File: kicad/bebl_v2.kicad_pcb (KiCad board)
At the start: 2 copper layers, 80 x 39 mm, 78 parts, among them P1 ISP, P10 LED_DRL, P11 DRV_LED, P12 CHG_LED, P13 LED_CHG, P2 FTDI, P3 LiPo, P4 USB-Micro, P5 Alt_Add, P6 Int1, P7 Int2, P8 DRL_LED, P9 LED_DRV, SW1 RST, SW2 MODE, U1 ATMEGA328, U2 FAN5346, U3 ADXL345, U4 MCP73831, U5 TPS61221DCK, X1 8MHz

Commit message: bebl_v2 3d of housing, work in progress
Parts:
- moved P3 6.02 mm to (99.5, 42.5), turned to 270 degrees
- moved SC1 0.71 mm to (40.5, 59.5)
- moved SC10 0.71 mm to (55.0, 74.5)
- moved SC11 0.71 mm to (110.0, 74.5)
- moved SC12 0.71 mm to (110.0, 65.5)
- moved SC2 0.71 mm to (115.5, 40.5)
- moved SC3 0.71 mm to (115.5, 59.5)
- moved SC4 0.71 mm to (40.5, 40.5)
- moved SC5 0.71 mm to (55.0, 54.5)
- moved SC6 0.71 mm to (55.0, 45.5)
- moved SC7 0.71 mm to (110.0, 45.5)
- moved SC8 0.71 mm to (110.0, 54.5)
- moved SC9 0.71 mm to (55.0, 65.5)
- moved B14 0.50 mm to (97.5, 50.0)
- moved B15 0.50 mm to (50.5, 50.0)
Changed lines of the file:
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@@
-(kicad_pcb (version 4) (host pcbnew "(2014-09-25 BZR 5147)-product")
+(kicad_pcb (version 4) (host pcbnew "(2014-jul-16 BZR unknown)-product")
   (general
     (links 143)
     (no_connects 143)
-    (area 37.8537 37.5442 118.521201 77.075001)
+    (area 36.399999 35.7817 119.600001 77.075001)
     (thickness 1.6)
-    (drawings 12)
+    (drawings 24)
     (tracks 0)
     (zones 0)
@@
   )
   (module bebl_v2_pretty:batt_clip (layer B.Cu)
-    (at 98 50 180)
+    (at 97.5 50 180)
     (fp_text reference B14 (at 3.556 0 450) (layer B.SilkS)
       (effects (font (size 1.5 1.5) (thickness 0.15)) (justify mirror))
@@
   )
   (module bebl_v2_pretty:batt_clip (layer B.Cu)
-    (at 50 50)
+    (at 50.5 50)
     (fp_text reference B15 (at 3.556 0 270) (layer B.SilkS)
       (effects (font (size 1.5 1.5) (thickness 0.15)) (justify mirror))
@@
   )
   (module bebl_v2_pretty:screw_3mm (layer F.Cu)
-    (at 110.5 65)
+    (at 110 65.5)
     (descr "vite 2,5mm")
     (fp_text reference SC12 (at 0 1.0795) (layer F.SilkS) hide
@@
   )
   (module bebl_v2_pretty:screw_3mm (layer F.Cu)
-    (at 110.5 75)
+    (at 110 74.5)
     (descr "vite 2,5mm")
     (fp_text reference SC11 (at 0 1.0795) (layer F.SilkS) hide
@@
   )
   (module bebl_v2_pretty:screw_3mm (layer F.Cu)
-    (at 54.5 75)
+    (at 55 74.5)
     (descr "vite 2,5mm")
     (fp_text reference SC10 (at 0 1.0795) (layer F.SilkS) hide
@@
   )
   (module bebl_v2_pretty:screw_3mm (layer F.Cu)
-    (at 54.5 65)
+    (at 55 65.5)
     (descr "vite 2,5mm")
     (fp_text reference SC9 (at 0 1.0795) (layer F.SilkS) hide
@@
   )
   (module bebl_v2_pretty:screw_3mm (layer F.Cu)
-    (at 110.5 55)
+    (at 110 54.5)
     (descr "vite 2,5mm")
     (fp_text reference SC8 (at 0 1.0795) (layer F.SilkS) hide
@@
   )
   (module bebl_v2_pretty:screw_3mm (layer F.Cu)
-    (at 110.5 45)
+    (at 110 45.5)
     (descr "vite 2,5mm")
     (fp_text reference SC7 (at 0 1.0795) (layer F.SilkS) hide
@@
   )
   (module bebl_v2_pretty:screw_3mm (layer F.Cu)
-    (at 54.5 45)
+    (at 55 45.5)
     (descr "vite 2,5mm")
     (fp_text reference SC6 (at 0 1.0795) (layer F.SilkS) hide
@@
   )
   (module bebl_v2_pretty:screw_3mm (layer F.Cu)
-    (at 54.5 55)
+    (at 55 54.5)
     (descr "vite 2,5mm")
     (fp_text reference SC5 (at 0 1.0795) (layer F.SilkS) hide
@@
   )
   (module bebl_v2_pretty:screw_3mm (layer F.Cu)
-    (at 40 60)
+    (at 40.5 59.5)
     (descr "vite 2,5mm")
     (fp_text reference SC1 (at 0 1.0795) (layer F.SilkS) hide
@@
   )
   (module bebl_v2_pretty:screw_3mm (layer F.Cu)
-    (at 116 40)
+    (at 115.5 40.5)
     (descr "vite 2,5mm")
     (fp_text reference SC2 (at 0 1.0795) (layer F.SilkS) hide
@@
   )
   (module bebl_v2_pretty:screw_3mm (layer F.Cu)
-    (at 116 60)
+    (at 115.5 59.5)
     (descr "vite 2,5mm")
     (fp_text reference SC3 (at 0 1.0795) (layer F.SilkS) hide
@@
   )
   (module bebl_v2_pretty:screw_3mm (layer F.Cu)
-    (at 40 40)
+    (at 40.5 40.5)
     (descr "vite 2,5mm")
     (fp_text reference SC4 (at 0 1.0795) (layer F.SilkS) hide
@@
   )
   (module bebl_v2_pretty:CONN_JST-2_SMD (layer F.Cu)
-    (at 104 38.5 180)
+    (at 99.5 42.5 270)
     (tags JST)
-    (fp_text reference P3 (at -5.5245 -7.747 450) (layer F.SilkS)
+    (fp_text reference P3 (at -5.5245 -7.747 540) (layer F.SilkS)
       (effects (font (size 1.016 1.016) (thickness 0.1524)))
     )
-    (fp_text value LiPo (at -5.5245 -2.9845 450) (layer F.SilkS)
+    (fp_text value LiPo (at -5.5245 -2.9845 540) (layer F.SilkS)
       (effects (font (size 1.016 1.016) (thickness 0.1524)))
     )
@@
     (fp_line (start 3.4925 -8.5725) (end 4.445 -8.5725) (layer F.SilkS) (width 0.1524))
     (fp_line (start 4.445 0.381) (end 0 0.381) (layer F.SilkS) (width 0.1524))
-    (pad "" smd rect (at -3.34772 -1.69926 180) (size 1.4986 3.39598) (layers F.Cu F.Paste F.Mask))
-    (pad 1 smd rect (at -0.99822 -7.24916 180) (size 0.99568 3.49758) (layers F.Cu F.Paste F.Mask)
+    (pad "" smd rect (at -3.34772 -1.69926 270) (size 1.4986 3.39598) (layers F.Cu F.Paste F.Mask))
+    (pad 1 smd rect (at -0.99822 -7.24916 270) (size 0.99568 3.49758) (layers F.Cu F.Paste F.Mask)
       (net 13 /BAT))
-    (pad 2 smd rect (at 0.99822 -7.24916 180) (size 0.99568 3.49758) (layers F.Cu F.Paste F.Mask)
-      (net 14 GND))
-    (pad "" smd rect (at 3.34772 -1.69926 180) (size 1.4986 3.39598) (layers F.Cu F.Paste F.Mask))
+    (pad 2 smd rect (at 0.99822 -7.24916 270) (size 0.99568 3.49758) (layers F.Cu F.Paste F.Mask)
+      (net 14 GND))
+    (pad "" smd rect (at 3.34772 -1.69926 270) (size 1.4986 3.39598) (layers F.Cu F.Paste F.Mask))
     (model /home/samata/projects-git/bebl_v2/kicad/3d_modules/s2b-ph-sm4-tb.wrl
       (at (xyz 0 0.254 0))
@@
     )
   )
+  (gr_line (start 38 43) (end 38 38) (angle 90) (layer Dwgs.User) (width 0.2))
+  (gr_line (start 43 43) (end 38 43) (angle 90) (layer Dwgs.User) (width 0.2))
+  (gr_line (start 43 38) (end 43 43) (angle 90) (layer Dwgs.User) (width 0.2))
+  (gr_line (start 38 38) (end 43 38) (angle 90) (layer Dwgs.User) (width 0.2))
+  (gr_line (start 118 38) (end 113 38) (angle 90) (layer Dwgs.User) (width 0.2))
+  (gr_line (start 118 43) (end 118 38) (angle 90) (layer Dwgs.User) (width 0.2))
+  (gr_line (start 113 43) (end 118 43) (angle 90) (layer Dwgs.User) (width 0.2))
+  (gr_line (start 113 38) (end 113 43) (angle 90) (layer Dwgs.User) (width 0.2))
+  (gr_line (start 119.5 63.5) (end 119.5 36.5) (angle 90) (layer Dwgs.User) (width 0.2))
+  (gr_line (start 36.5 63.5) (end 119.5 63.5) (angle 90) (layer Dwgs.User) (width 0.2))
+  (gr_line (start 36.5 36.5) (end 36.5 63.5) (angle 90) (layer Dwgs.User) (width 0.2))
+  (gr_line (start 119.5 36.5) (end 36.5 36.5) (angle 90) (layer Dwgs.User) (width 0.2))
   (gr_line (start 52.5 63) (end 77.5 63) (angle 90) (layer Edge.Cuts) (width 0.15))
   (gr_line (start 77.5 62) (end 38 62) (angle 90) (layer Edge.Cuts) (width 0.15))

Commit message: working on case for bebl_v2
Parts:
- removed B8, B9: I/O, bebl_v2_pretty:breakout_smd
- removed P5: Alt_Add, bebl_v2_pretty:solder_bridge_3
- removed P6: Int1, bebl_v2_pretty:solder_bridge_3
- removed P7: Int2, bebl_v2_pretty:solder_bridge_3
- moved P3 12.0 mm to (87.5, 42.5)
- moved P1 4.00 mm to (67.5, 39.5)
- moved R1 4.00 mm to (87.0, 60.0)
- moved C12 3.50 mm to (83.0, 53.5)
- moved C8 3.50 mm to (91.0, 53.5)
- moved R6 3.50 mm to (87.0, 57.0)
- moved R7 3.50 mm to (87.0, 50.0)
- moved U4 3.50 mm to (87.0, 53.5)
- moved C10 2.00 mm to (77.0, 49.0)
- moved C7 2.00 mm to (77.0, 55.0)
- moved L2 2.00 mm to (72.5, 52.0)
- moved U5 2.00 mm to (77.0, 52.0)
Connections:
- P4 pad 2: Net-(P4-Pad2) -> (no net)
- P4 pad 3: Net-(P4-Pad3) -> (no net)
- P4 pad 4: Net-(P4-Pad4) -> (no net)
- R8 pad 2: /INT0 -> /MODE
- SW2 pad 2: /INT0 -> /MODE
- U1 pad 1: Net-(B8-Pad1) -> /ACL_INT2
- U1 pad 2: Net-(B9-Pad1) -> /MODE
- U1 pad 32: /INT0 -> /ACL_INT1
- U3 pad 10: Net-(U3-Pad10) -> (no net)
- U3 pad 11: Net-(U3-Pad11) -> (no net)
- U3 pad 12: /ACL_SDO -> GND
- U3 pad 3: Net-(U3-Pad3) -> (no net)

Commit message: bebl_v2 track layout, work in progress
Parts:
- removed B1, B10, B11, B12, B13, B2, B3, B4, B5, B6: I/O, bebl_v2_pretty:breakout_smd
- removed SC10, SC11, SC12, SC9: SCREW, bebl_v2_pretty:screw_3mm
- P3: footprint bebl_v2_pretty:CONN_JST-2_SMD -> bebl_v2_pretty:pin_strip_2
- moved C3 20.8 mm to (60.5, 58.0), turned to 0 degrees
- moved R2 18.1 mm to (79.5, 41.0), turned to 90 degrees
- moved P9 17.6 mm to (37.0, 72.0)
- moved P11 17.5 mm to (37.0, 50.0)
- moved P8 17.4 mm to (93.5, 46.5)
- moved P10 17.1 mm to (93.5, 68.5)
- moved D6 16.1 mm to (44.0, 72.0)
- moved SC5 15.2 mm to (40.0, 57.0)
- moved SC6 15.2 mm to (40.0, 43.0)
- moved R3 14.8 mm to (82.0, 41.0), turned to 90 degrees
- moved R4 14.2 mm to (88.5, 56.5)
- moved D5 13.6 mm to (54.0, 72.0)
- moved C4 12.5 mm to (79.5, 55.5)
- moved R6 12.2 mm to (78.5, 48.2)
- moved D4 11.2 mm to (64.0, 72.0)
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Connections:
- P4 pad 2: (no net) -> Net-(P4-Pad2)
- P4 pad 3: (no net) -> Net-(P4-Pad3)
- P4 pad 4: (no net) -> Net-(P4-Pad4)
- U1 pad 1: /ACL_INT2 -> /ACL_INT1
- U1 pad 32: /ACL_INT1 -> /ACL_INT2
- U3 pad 10: (no net) -> Net-(U3-Pad10)
- U3 pad 11: (no net) -> Net-(U3-Pad11)
- U3 pad 3: (no net) -> Net-(U3-Pad3)
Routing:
- net GND: track 0.00 -> 245.7 mm, vias 0 -> 5
- net +3.3V: track 0.00 -> 106.4 mm, vias 0 -> 2
- net /BAT: track 0.00 -> 71.2 mm, vias 0 -> 1
- net /CATH: track 0.00 -> 48.8 mm
- net /RESET: track 0.00 -> 40.8 mm, vias 0 -> 2
- net /VUSB: track 0.00 -> 33.8 mm
- net /MODE: track 0.00 -> 26.8 mm, vias 0 -> 1
- net /LED_A: track 0.00 -> 26.5 mm
- net /DRL_PWM: track 0.00 -> 25.5 mm, vias 0 -> 2
- net /LED_K: track 0.00 -> 25.4 mm
- net Net-(P12-Pad2): track 0.00 -> 20.9 mm
- net /SCL: track 0.00 -> 20.1 mm, vias 0 -> 2
- net /PB7: track 0.00 -> 19.0 mm
- net /ACL_INT1: track 0.00 -> 18.5 mm, vias 0 -> 2
- net /PB6: track 0.00 -> 17.1 mm
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- added copper zone on B.Cu, net GND
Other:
- board size 80 x 39 mm -> 80 x 41 mm
- net class 0.2mm added: clearance 0.2, trace_width 0.2, via_dia 0.889, via_drill 0.635
- net class Default: clearance 0.254 -> 0.25; trace_width 0.254 -> 0.3
- rule trace_clearance: 0.254 -> 0.25
- rule trace_min: 0.254 -> 0.2

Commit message: working on case for bebl_v2
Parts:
- added B1: I/O, bebl_v2_pretty:breakout_smd, B.Cu at (75.1, 43.1)
- added B10: I/O, bebl_v2_pretty:breakout_smd, B.Cu at (64.9, 51.0)
- added B11: I/O, bebl_v2_pretty:breakout_smd, B.Cu at (64.0, 49.8)
- added B12: I/O, bebl_v2_pretty:breakout_smd, B.Cu at (63.4, 48.4)
- added B13: I/O, bebl_v2_pretty:breakout_smd, B.Cu at (63.3, 46.9)
- added B2: I/O, bebl_v2_pretty:breakout_smd, B.Cu at (76.6, 43.1)
- added B3: I/O, bebl_v2_pretty:breakout_smd, B.Cu at (77.9, 45.3)
- added B4: I/O, bebl_v2_pretty:breakout_smd, B.Cu at (77.9, 46.8)
- added B5: I/O, bebl_v2_pretty:breakout_smd, B.Cu at (69.6, 43.5)
- added B6: I/O, bebl_v2_pretty:breakout_smd, B.Cu at (73.6, 43.1)
- P3: value LiPo -> Ext_LiPo; moved to B.Cu
- moved R7 3.00 mm to (78.5, 48.5)
- moved R6 2.70 mm to (78.5, 45.5)
- moved U4 2.50 mm to (78.5, 52.0)
- moved C4 1.58 mm to (80.0, 57.0), turned to 180 degrees
- moved C12 1.50 mm to (74.5, 52.0)
- moved C6 0.50 mm to (55.0, 53.0)
- moved R4 0.50 mm to (88.5, 57.0)
- moved R5 0.50 mm to (55.0, 47.0)
- moved L1 0.40 mm to (62.0, 52.1)
- moved C8 0.30 mm to (82.5, 52.0)
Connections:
- C5 pad 1: /VLED -> +3.3V
- L1 pad 1: /VLED -> +3.3V
- P4 pad 2: Net-(P4-Pad2) -> (no net)
- P4 pad 3: Net-(P4-Pad3) -> (no net)
- P4 pad 4: Net-(P4-Pad4) -> (no net)
- U2 pad 1: /VLED -> +3.3V
- U3 pad 10: Net-(U3-Pad10) -> (no net)
- U3 pad 11: Net-(U3-Pad11) -> (no net)
- U3 pad 3: Net-(U3-Pad3) -> (no net)
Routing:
- net GND: track 245.7 -> 283.8 mm
- net /ACL_INT2: track 0.00 -> 15.3 mm, vias 0 -> 2
- net +3.3V: track 106.4 -> 115.3 mm
- net /VLED: track 5.77 -> 0.00 mm
- net Net-(B1-Pad1): track 0.00 -> 4.50 mm
- net Net-(B2-Pad1): track 0.00 -> 4.41 mm
- net /SS: track 0.00 -> 4.34 mm
- net Net-(B3-Pad1): track 0.00 -> 4.04 mm
- net Net-(B12-Pad1): track 0.00 -> 3.95 mm
- net Net-(B4-Pad1): track 0.00 -> 3.66 mm
- net Net-(B6-Pad1): track 0.00 -> 3.33 mm
- net Net-(B11-Pad1): track 0.00 -> 3.10 mm
- net /ACL_INT1: track 18.5 -> 15.5 mm
- net Net-(P12-Pad2): track 20.9 -> 23.4 mm
- net /SDA: track 16.4 -> 13.9 mm
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- added copper zone on F.Cu, net /D1K
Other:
- board text added: "(3V3)"
- board text added: "BLK"
- board text added: "BicyclE Brake Light"
- board text added: "GRN"
- board text added: "[+ -]"
- board text added: "[+]"
- board text added: "[-]"
- board text added: "bebl_v2"
- board text added: "www.wyolum.com"

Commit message: work in progress
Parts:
- moved D1 3.00 mm to (104.0, 75.0)
- moved D2 3.00 mm to (84.0, 75.0)
- moved D3 3.00 mm to (74.0, 75.0)
- moved D4 3.00 mm to (64.0, 75.0)
- moved D5 3.00 mm to (54.0, 75.0)
- moved D6 3.00 mm to (44.0, 75.0)
- moved D8 3.00 mm to (94.0, 75.0)
- moved P10 3.00 mm to (93.5, 71.5)
- moved P13 3.00 mm to (93.5, 78.5)
- moved P9 3.00 mm to (37.0, 75.0)
- turned P3 to 180 degrees
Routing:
- net /BAT: track 72.4 -> 67.4 mm
- net GND: track 283.8 -> 285.9 mm
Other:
- board size 80 x 41 mm -> 80 x 44 mm
- board text added: "[- +]"
- board text removed: "[+ -]"

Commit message: bebl_v2 box stl files ready for prototype
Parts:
- moved P4 0.10 mm to (109.9, 50.0)

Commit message: modified schematic for transistor drive
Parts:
- renumbered P4 to P7, P12 to P8

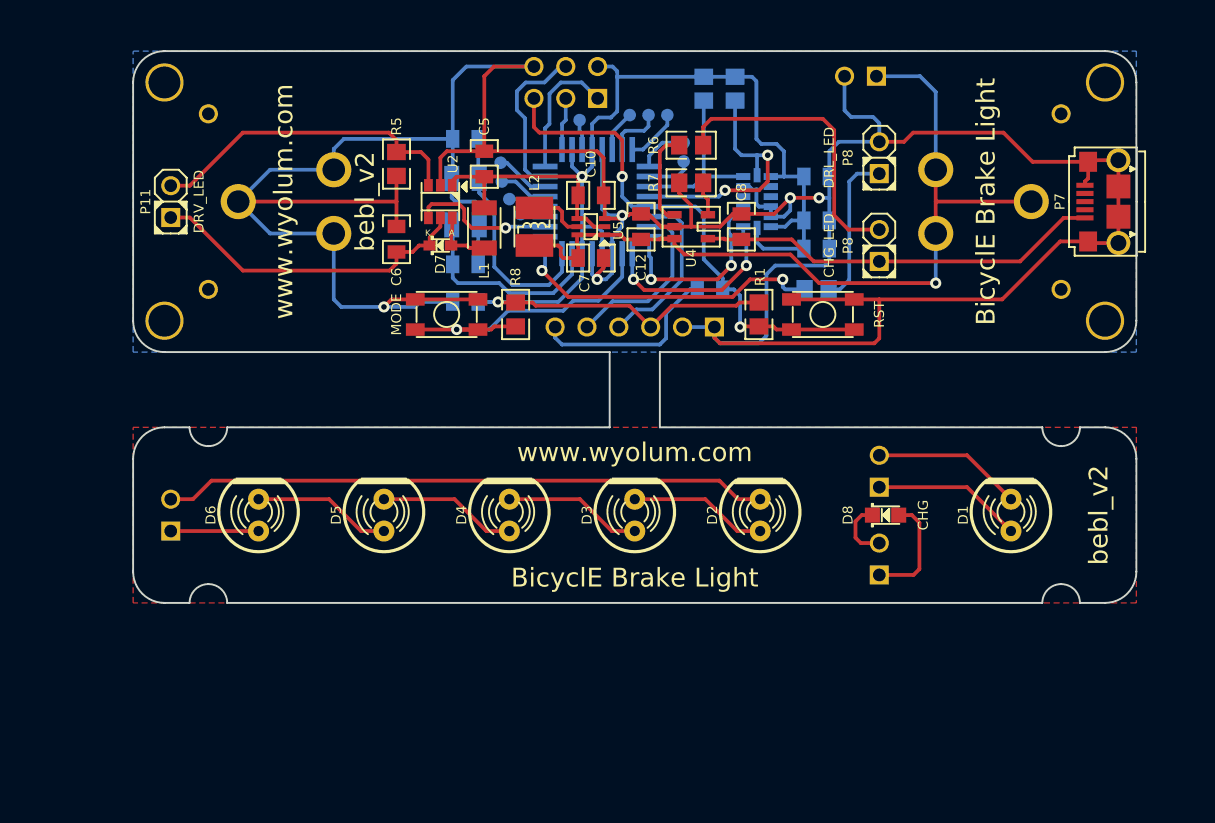
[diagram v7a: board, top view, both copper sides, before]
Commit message: new LED drive circuit, work in progress
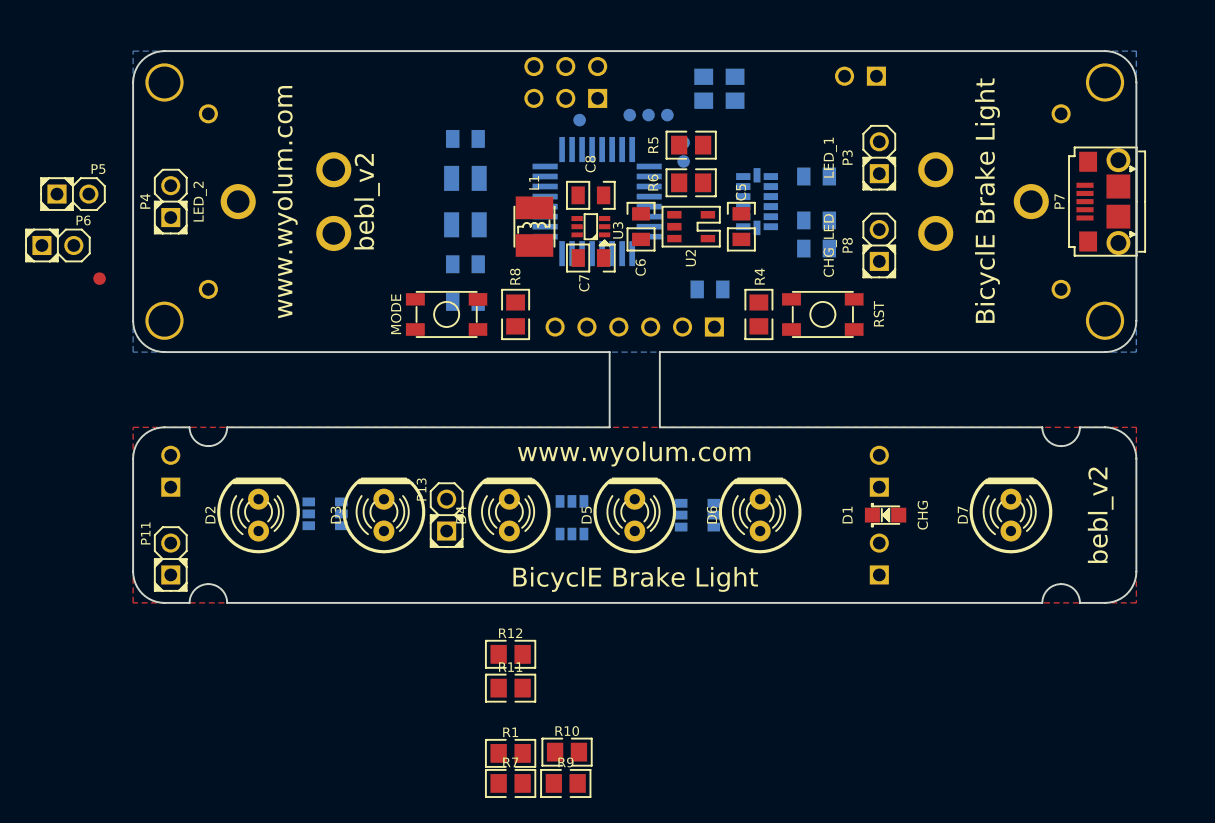
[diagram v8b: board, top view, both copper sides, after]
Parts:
- removed B10, B11, B12, B13: I/O, bebl_v2_pretty:breakout_smd
- removed the C5 at (62.0, 47.0)
- removed the C6 at (55.0, 53.0)
- removed the D7 at (58.5, 53.5)
- removed the L1 at (62.0, 52.1)
- removed the P3 at (92.0, 40.0)
- removed the R4 at (88.5, 57.0)
- removed the R5 at (55.0, 47.0)
- removed the U2 at (58.5, 50.0)
- added B7: I/O, bebl_v2_pretty:breakout_smd, F.Cu at (31.3, 56.1)
- added P10: LED_CHG, bebl_v2_pretty:pin_strip_2, B.Cu at (93.5, 78.5)
- added P11: LED_1, bebl_v2_pretty:pin_strip_2, F.Cu at (37.0, 78.5)
- added P12: LED_2, bebl_v2_pretty:pin_strip_2, B.Cu at (37.0, 71.5)
- added P5: LED_3, bebl_v2_pretty:pin_socket_2, F.Cu at (29.2, 49.4)
- added P6: LED_PWR, bebl_v2_pretty:pin_socket_2, F.Cu at (28.0, 53.5)
- added Q1: BC847BDW1T1G, bebl_v2_pretty:SOT23-6, B.Cu at (79.0, 75.0)
- added Q2: BC847BDW1T1G, bebl_v2_pretty:SOT23-6, B.Cu at (49.3, 74.9)
- added Q3: BC847BDW1T1G, bebl_v2_pretty:SOT23-6, B.Cu at (69.0, 75.2)
- added R1: 10k, bebl_v2_pretty:r_0805, F.Cu at (64.1, 94.0)
- added R10: 56E, bebl_v2_pretty:r_0805, F.Cu at (68.6, 93.9)
- added R11: 56E, bebl_v2_pretty:r_0805, F.Cu at (64.1, 88.8)
- added R12: 56E, bebl_v2_pretty:r_0805, F.Cu at (64.1, 86.1)
- added R7: 56E, bebl_v2_pretty:r_0805, F.Cu at (64.1, 96.4)
- added R9: 56E, bebl_v2_pretty:r_0805, F.Cu at (68.5, 96.4)
- D2: renamed from D6; value LED_R -> LED_P
- D3: renamed from D5; value LED_R -> LED_P
- D4: value LED_R -> LED_P
- D5: renamed from D3; value LED_R -> LED_P
- D6: renamed from D2; value LED_R -> LED_B
- D7: renamed from D1; value DRL -> LED_D
- P13: value LED_CHG -> LED_3; moved to F.Cu
- P14: renamed from P10; value LED_DRL -> LED_PWR
- P3: renamed from P8; value DRL_LED -> LED_1
- P4: renamed from P11; value DRV_LED -> LED_2
- P9: value LED_DRV -> Ext_LiPo; footprint bebl_v2_pretty:pin_strip_2 -> bebl_v2_pretty:pin_socket_2
- R8: value 10k -> 56E
- moved P9 65.2 mm to (92.0, 40.0), turned to 180 degrees
- moved P13 34.7 mm to (59.0, 75.0)
- renumbered B14 to B8, B15 to B9, C13 to C10, C8 to C5, C12 to C6, C10 to C8, D8 to D1, L2 to L1, R1 to R4, R6 to R5, R7 to R6, U4 to U2, U5 to U3, U3 to U4
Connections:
- D1 pad 1: Net-(D8-Pad1) -> Net-(D1-Pad1)
- D1 pad 2: Net-(D8-Pad2) -> Net-(D1-Pad2)
- D2 pad 1: /ANOD -> Net-(D6-Pad1)
- D2 pad 2: Net-(D5-Pad1) -> Net-(D6-Pad2)
- D3 pad 2: Net-(D4-Pad1) -> Net-(D5-Pad2)
- D4 pad 2: Net-(D3-Pad1) -> Net-(D4-Pad2)
- D5 pad 2: Net-(D2-Pad1) -> Net-(D3-Pad2)
- D6 pad 2: /CATH -> Net-(D2-Pad2)
- D7 pad 1: /D1A -> Net-(D7-Pad1)
- D7 pad 2: /D1K -> Net-(D7-Pad2)
- P13 pad 1: Net-(D8-Pad1) -> Net-(P13-Pad1)
- P13 pad 2: Net-(D8-Pad2) -> Net-(P13-Pad2)
- P14 pad 1: /D1A -> /LED_brd/3V3_LED
- P14 pad 2: /D1K -> GND
- P3 pad 1: /DRL -> /SCK
- P3 pad 2: GND -> Net-(P3-Pad2)
- P4 pad 1: /LED_A -> Net-(P4-Pad1)
- P4 pad 2: /LED_K -> Net-(P4-Pad2)
- P9 pad 1: /ANOD -> /BAT
- P9 pad 2: /CATH -> GND
- R4 pad 2: /RESET -> /MODE
- R8 pad 1: +3.3V -> Net-(D3-Pad1)
- R8 pad 2: /MODE -> /LED_brd/3V3_LED
- U1 pad 10: /LED_PWM -> Net-(P4-Pad1)
- U1 pad 13: Net-(B12-Pad1) -> Net-(P4-Pad2)
- U1 pad 9: /DRL_PWM -> Net-(P3-Pad2)
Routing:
- net GND: track 285.7 -> 0.00 mm, vias 5 -> 0
- net +3.3V: track 115.3 -> 0.00 mm, vias 2 -> 0
- net /BAT: track 67.4 -> 0.00 mm, vias 1 -> 0
- net /CATH: track 48.2 -> 0.00 mm
- net /RESET: track 41.3 -> 0.00 mm, vias 2 -> 0
- net /VUSB: track 32.3 -> 0.00 mm
- net /MODE: track 26.6 -> 0.00 mm, vias 1 -> 0
- net /LED_A: track 26.4 -> 0.00 mm
- net /DRL_PWM: track 25.9 -> 0.00 mm, vias 2 -> 0
- net /LED_K: track 25.8 -> 0.00 mm
- net Net-(P8-Pad2): track 23.4 -> 0.00 mm
- net /SCL: track 20.3 -> 0.00 mm, vias 2 -> 0
- net /PB7: track 18.6 -> 0.00 mm
- net /PB6: track 16.6 -> 0.00 mm
- net /ACL_INT1: track 15.5 -> 0.00 mm, vias 2 -> 0
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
